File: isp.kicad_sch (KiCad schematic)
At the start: 4 parts, among them J1 AVR-ISP-6, SW1 SW_Push, U2 PRO_MICRO

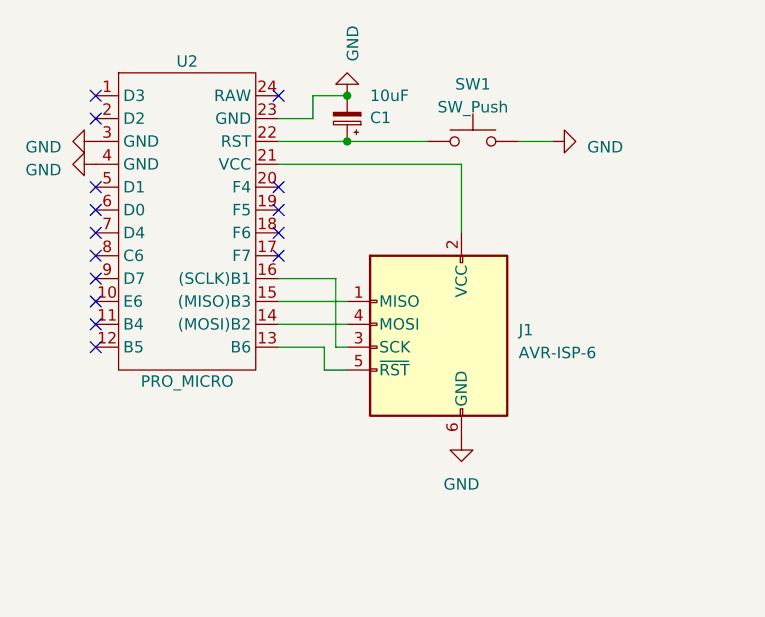
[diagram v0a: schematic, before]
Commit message: add breakout header
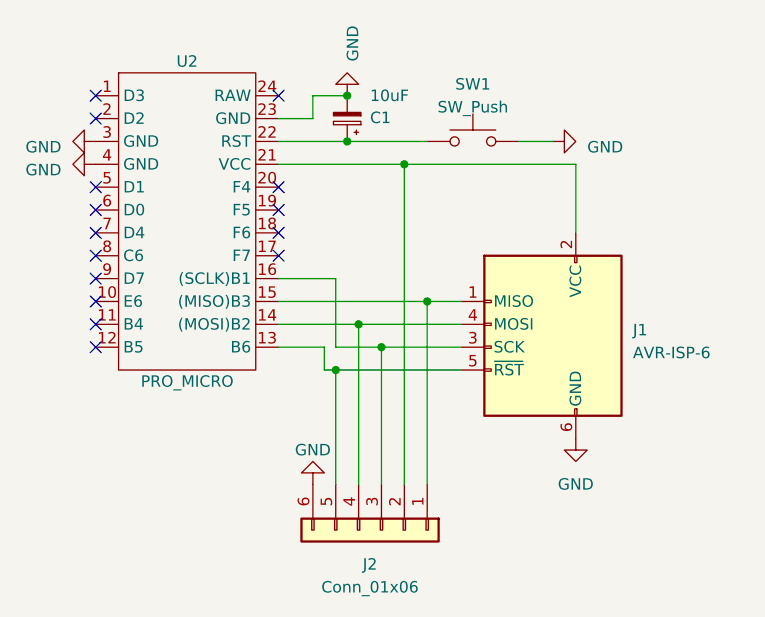
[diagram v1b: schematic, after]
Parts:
- added J2: Conn_01x06, Connector_PinHeader_2.54mm:PinHeader_1x06_P2.54mm_Vertical, symbol Connector_Generic:Conn_01x06
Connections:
- net GND: now also J2.6 (Pin_6)
- net at J1.5 (~{RST}), U2.13 (B6): now also J2.5 (Pin_5)
- net at J1.4 (MOSI), U2.14 ((MOSI)B2): now also J2.4 (Pin_4)
- net at J1.1 (MISO), U2.15 ((MISO)B3): now also J2.1 (Pin_1)
- net at J1.3 (SCK), U2.16 ((SCLK)B1): now also J2.3 (Pin_3)
- net at J1.2 (VCC), U2.21 (VCC): now also J2.2 (Pin_2)
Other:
- moved on the sheet: J1
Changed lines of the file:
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@@
 (kicad_sch (version 20230121) (generator eeschema)
   (paper "A4")
+  (junction (at 106.68 93.98) (diameter 0) (color 0 0 0 0)
+  )
+  (junction (at 104.14 91.44) (diameter 0) (color 0 0 0 0)
+  )
   (junction (at 102.87 66.04) (diameter 0) (color 0 0 0 0)
   )
+  (junction (at 101.6 96.52) (diameter 0) (color 0 0 0 0)
+  )
+  (junction (at 111.76 88.9) (diameter 0) (color 0 0 0 0)
+  )
   (junction (at 102.87 71.12) (diameter 0) (color 0 0 0 0)
+  )
+  (junction (at 109.22 73.66) (diameter 0) (color 0 0 0 0)
   )
   (no_connect (at 95.25 66.04))
@@
   (no_connect (at 74.93 68.58))
   (no_connect (at 74.93 88.9))
+  (wire (pts (xy 101.6 96.52) (xy 101.6 109.22))
+    (stroke (width 0) (type default))
+  )
   (wire (pts (xy 102.87 71.12) (xy 111.76 71.12))
     (stroke (width 0) (type default))
@@
     (stroke (width 0) (type default))
   )
-  (wire (pts (xy 115.57 73.66) (xy 115.57 81.28))
+  (wire (pts (xy 128.27 73.66) (xy 128.27 81.28))
+    (stroke (width 0) (type default))
+  )
+  (wire (pts (xy 104.14 91.44) (xy 115.57 91.44))
     (stroke (width 0) (type default))
   )
@@
     (stroke (width 0) (type default))
   )
-  (wire (pts (xy 95.25 88.9) (xy 102.87 88.9))
+  (wire (pts (xy 95.25 88.9) (xy 111.76 88.9))
     (stroke (width 0) (type default))
   )
@@
     (stroke (width 0) (type default))
   )
-  (wire (pts (xy 101.6 93.98) (xy 102.87 93.98))
-    (stroke (width 0) (type default))
-  )
-  (wire (pts (xy 95.25 91.44) (xy 102.87 91.44))
+  (wire (pts (xy 101.6 93.98) (xy 106.68 93.98))
+    (stroke (width 0) (type default))
+  )
+  (wire (pts (xy 95.25 91.44) (xy 104.14 91.44))
     (stroke (width 0) (type default))
   )
@@
     (stroke (width 0) (type default))
   )
-  (wire (pts (xy 100.33 96.52) (xy 102.87 96.52))
-    (stroke (width 0) (type default))
-  )
-  (wire (pts (xy 95.25 73.66) (xy 115.57 73.66))
+  (wire (pts (xy 100.33 96.52) (xy 101.6 96.52))
+    (stroke (width 0) (type default))
+  )
+  (wire (pts (xy 95.25 73.66) (xy 109.22 73.66))
+    (stroke (width 0) (type default))
+  )
+  (wire (pts (xy 101.6 96.52) (xy 115.57 96.52))
+    (stroke (width 0) (type default))
+  )
+  (wire (pts (xy 106.68 93.98) (xy 115.57 93.98))
+    (stroke (width 0) (type default))
+  )
+  (wire (pts (xy 111.76 88.9) (xy 115.57 88.9))
+    (stroke (width 0) (type default))
+  )
+  (wire (pts (xy 111.76 88.9) (xy 111.76 109.22))
     (stroke (width 0) (type default))
   )
@@
     (stroke (width 0) (type default))
   )
+  (wire (pts (xy 109.22 73.66) (xy 109.22 109.22))
+    (stroke (width 0) (type default))
+  )
+  (wire (pts (xy 106.68 93.98) (xy 106.68 109.22))
+    (stroke (width 0) (type default))
+  )
   (wire (pts (xy 100.33 93.98) (xy 100.33 96.52))
     (stroke (width 0) (type default))
   )
+  (wire (pts (xy 104.14 91.44) (xy 104.14 109.22))
+    (stroke (width 0) (type default))
+  )
+  (wire (pts (xy 109.22 73.66) (xy 128.27 73.66))
+    (stroke (width 0) (type default))
+  )
   (wire (pts (xy 95.25 68.58) (xy 99.06 68.58))
     (stroke (width 0) (type default))
   )
-  (symbol (lib_id "power:GND") (at 115.57 104.14 0) (mirror y) (unit 1)
-    (in_bom yes) (on_board yes) (dnp no) (fields_autoplaced)
-    (property "Reference" "#PWR04" (at 115.57 110.49 0)
-      (effects (font (size 1.27 1.27)) hide)
-    )
-    (property "Value" "GND" (at 115.57 109.22 0)
-      (effects (font (size 1.27 1.27)))
-    )
-    (property "Footprint" "" (at 115.57 104.14 0)
-      (effects (font (size 1.27 1.27)) hide)
-    )
-    (property "Datasheet" "" (at 115.57 104.14 0)
+  (symbol (lib_id "power:GND") (at 128.27 104.14 0) (mirror y) (unit 1)
+    (in_bom yes) (on_board yes) (dnp no) (fields_autoplaced)
+    (property "Reference" "#PWR04" (at 128.27 110.49 0)
+      (effects (font (size 1.27 1.27)) hide)
+    )
+    (property "Value" "GND" (at 128.27 109.22 0)
+      (effects (font (size 1.27 1.27)))
+    )
+    (property "Footprint" "" (at 128.27 104.14 0)
+      (effects (font (size 1.27 1.27)) hide)
+    )
+    (property "Datasheet" "" (at 128.27 104.14 0)
       (effects (font (size 1.27 1.27)) hide)
     )
@@
     )
   )
+  (symbol (lib_id "Connector_Generic:Conn_01x06") (at 106.68 114.3 270) (unit 1)
+    (in_bom yes) (on_board yes) (dnp no) (fields_autoplaced)
+    (property "Reference" "J2" (at 105.41 118.11 90)
+      (effects (font (size 1.27 1.27)))
+    )
+    (property "Value" "Conn_01x06" (at 105.41 120.65 90)
+      (effects (font (size 1.27 1.27)))
+    )
+    (property "Footprint" "Connector_PinHeader_2.54mm:PinHeader_1x06_P2.54mm_Vertical" (at 106.68 114.3 0)
+      (effects (font (size 1.27 1.27)) hide)
+    )
+    (property "Datasheet" "~" (at 106.68 114.3 0)
+      (effects (font (size 1.27 1.27)) hide)
+    )
+    (pin "1")
+    (pin "2")
+    (pin "3")
+    (pin "4")
+    (pin "5")
+    (pin "6")
+    (instances
+      (project "isp"
+        (path "/e810ca06-3074-4cfb-9e2e-5e2eef787eed"
+          (reference "J2") (unit 1)
+        )
+      )
+    )
+  )
   (symbol (lib_id "Switch:SW_Push") (at 116.84 71.12 0) (unit 1)
     (in_bom yes) (on_board yes) (dnp no) (fields_autoplaced)
@@
     )
   )
+  (symbol (lib_id "power:GND") (at 99.06 109.22 0) (mirror x) (unit 1)
+    (in_bom yes) (on_board yes) (dnp no) (fields_autoplaced)
+    (property "Reference" "#PWR06" (at 99.06 102.87 0)
+      (effects (font (size 1.27 1.27)) hide)
+    )
+    (property "Value" "GND" (at 99.06 105.41 0)
+      (effects (font (size 1.27 1.27)))
+    )
+    (property "Footprint" "" (at 99.06 109.22 0)
+      (effects (font (size 1.27 1.27)) hide)
+    )
+    (property "Datasheet" "" (at 99.06 109.22 0)
+      (effects (font (size 1.27 1.27)) hide)
+    )
+    (pin "1")
+    (instances
+      (project "isp"
+        (path "/e810ca06-3074-4cfb-9e2e-5e2eef787eed"
+          (reference "#PWR06") (unit 1)
+        )
+      )
+    )
+  )
   (symbol (lib_id "Device:C_Polarized_Small") (at 102.87 68.58 180) (unit 1)
     (in_bom yes) (on_board yes) (dnp no)
@@
     )
   )
-  (symbol (lib_id "Connector:AVR-ISP-6") (at 113.03 93.98 0) (mirror y) (unit 1)
-    (in_bom yes) (on_board yes) (dnp no) (fields_autoplaced)
-    (property "Reference" "J1" (at 121.92 92.075 0)
-      (effects (font (size 1.27 1.27)) (justify right))
-    )
-    (property "Value" "AVR-ISP-6" (at 121.92 94.615 0)
-      (effects (font (size 1.27 1.27)) (justify right))
-    )
-    (property "Footprint" "Connector_IDC:IDC-Header_2x03_P2.54mm_Vertical" (at 119.38 92.71 90)
-      (effects (font (size 1.27 1.27)) hide)
-    )
-    (property "Datasheet" " ~" (at 145.415 107.95 0)
-      (effects (font (size 1.27 1.27)) hide)
-    )
+  (symbol (lib_id "Connector:AVR-ISP-6") (at 125.73 93.98 0) (mirror y) (unit 1)
+    (in_bom yes) (on_board yes) (dnp no) (fields_autoplaced)
+    (property "Reference" "J1" (at 134.62 92.075 0)
+      (effects (font (size 1.27 1.27)) (justify right))
+    )
+    (property "Value" "AVR-ISP-6" (at 134.62 94.615 0)
+      (effects (font (size 1.27 1.27)) (justify right))
+    )
+    (property "Footprint" "Connector_IDC:IDC-Header_2x03_P2.54mm_Vertical" (at 132.08 92.71 90)
+      (effects (font (size 1.27 1.27)) hide)
+    )
+    (property "Datasheet" " ~" (at 158.115 107.95 0)
+      (effects (font (size 1.27 1.27)) hide)
+    )
